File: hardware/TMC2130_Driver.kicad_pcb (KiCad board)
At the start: 2 copper layers, 36.7 x 39.4 mm, 35 parts, among them J1 PCIe_Stepper, J2 Conn_01x04_Male, J3 Screw_Terminal_01x02, U1 TMC2130, U2 24LC02

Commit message: 2130 completed
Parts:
- moved LOGO1 30.2 mm to (116.2, 78.0)
- moved JP1 22.6 mm to (117.5, 96.4)
- moved J3 22.2 mm to (141.5, 101.0), turned to 90 degrees
- moved C15 22.0 mm to (129.7, 77.7)
- moved C13 21.2 mm to (139.0, 80.6), turned to -90 degrees
- moved F1 20.8 mm to (135.6, 102.1), turned to 180 degrees
- moved R2 20.0 mm to (125.4, 77.9), turned to 180 degrees
- moved C4 19.9 mm to (132.8, 77.8), turned to 90 degrees
- moved J2 19.0 mm to (141.5, 87.0), turned to 90 degrees
- moved C17 19.0 mm to (130.9, 78.2), turned to 90 degrees
- moved C11 18.7 mm to (137.3, 81.4), turned to -90 degrees
- moved C5 15.8 mm to (126.2, 100.8), turned to 180 degrees
- moved C9 15.7 mm to (131.1, 80.7), turned to 0 degrees
- moved C3 15.5 mm to (133.7, 81.8), turned to 135 degrees
- moved C8 15.3 mm to (136.2, 83.7), turned to 0 degrees
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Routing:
- net /V_IO: track 17.3 -> 43.3 mm
- net /SCK: track 16.0 -> 38.6 mm, vias 1 -> 3
- net /CLOCK: track 20.7 -> 42.5 mm
- net /~CS: track 16.3 -> 36.0 mm
- net /V_HIGH: track 92.3 -> 75.5 mm
- net /5V: track 53.7 -> 70.5 mm
- net /MOSI: track 18.0 -> 34.0 mm
- net /MISO: track 17.7 -> 33.5 mm
- net /STEP: track 20.8 -> 35.8 mm
- net /ALARM1: track 33.6 -> 19.2 mm
- net /DIR: track 22.0 -> 35.2 mm
- net Net-(JP1-Pad1): track 23.0 -> 33.4 mm
- net GND: track 69.1 -> 61.3 mm, vias 61 -> 57
- net Net-(JP1-Pad3): track 22.8 -> 29.8 mm
- net /ID_0: track 8.53 -> 15.4 mm
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
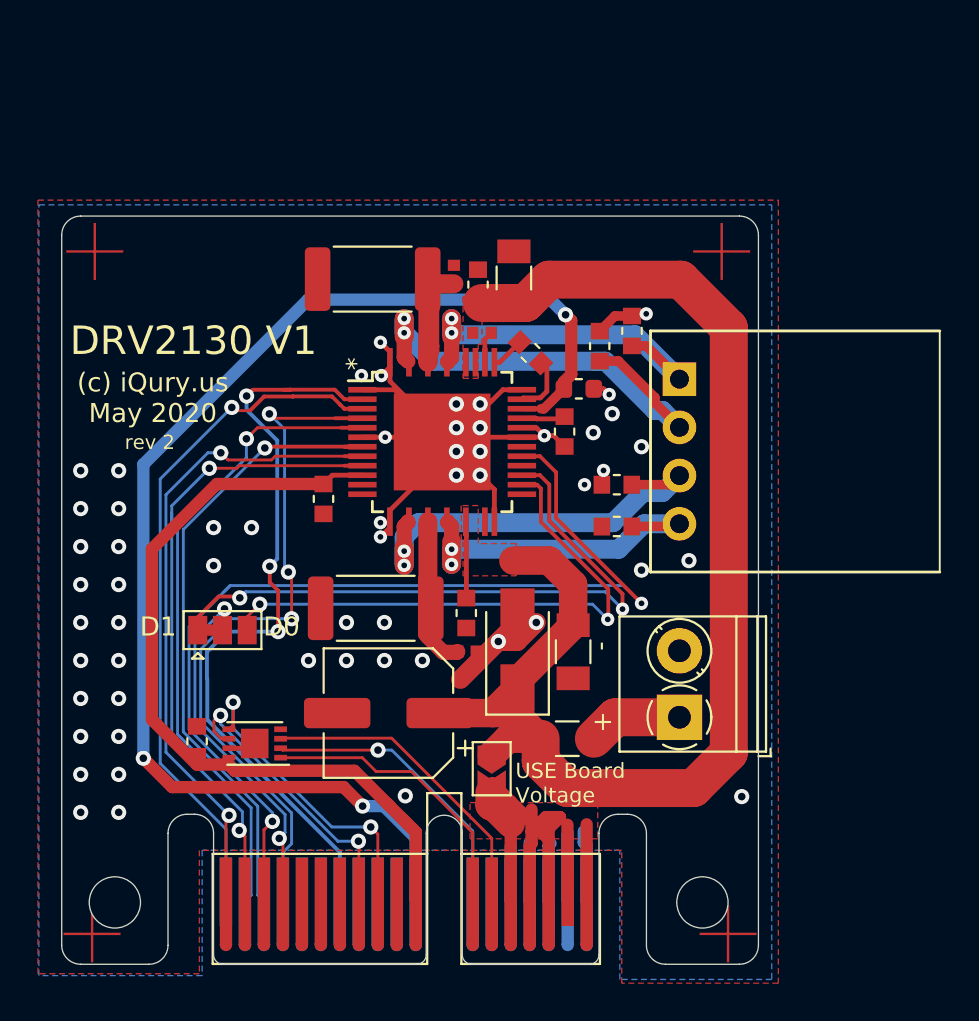
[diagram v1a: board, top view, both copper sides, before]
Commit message: Small correcion of 2130
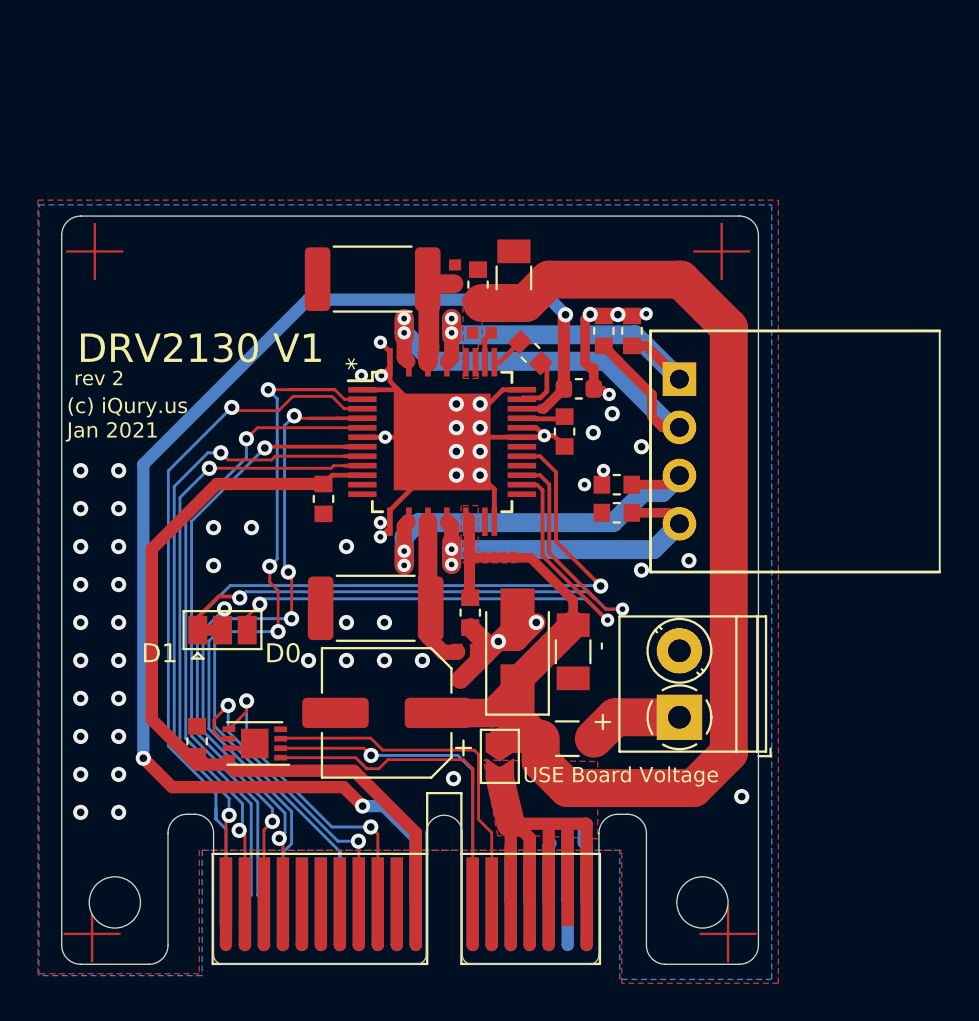
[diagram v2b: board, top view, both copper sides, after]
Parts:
- moved C11 0.83 mm to (137.6, 80.6)
- moved JP2 0.78 mm to (132.1, 103.0)
- moved C14 0.72 mm to (138.2, 90.2)
- moved C1 0.21 mm to (130.5, 95.5)
- moved C10 0.10 mm to (130.3, 97.4)
- moved C5 0.09 mm to (126.1, 100.8)
- moved C15 0.06 mm to (129.7, 77.7)
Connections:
- J1 pad : /STEP -> /CLOCK
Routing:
- net GND: track 61.3 -> 67.1 mm, vias 57 -> 60
- net /V_HIGH: track 75.5 -> 80.9 mm
- net /~ENABLE: track 53.0 -> 47.8 mm
- net /V_MOTORS: track 30.6 -> 27.4 mm
- net /ID_0: track 15.4 -> 18.5 mm
- net /5V: track 70.5 -> 67.7 mm
- net /ID_2: track 16.6 -> 18.8 mm
- net /SCK: track 38.6 -> 40.6 mm
- net /ID_1: track 15.6 -> 17.5 mm
- net /SCL: track 15.0 -> 16.4 mm
- net /V_IO: track 43.3 -> 42.0 mm
- net /DIR: track 35.2 -> 34.1 mm
- net /CLOCK: track 42.5 -> 43.4 mm
- net Net-(JP1-Pad1): track 33.4 -> 34.0 mm
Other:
- board text added: "(c) iQury.us Jan 2021"
- board text removed: "(c) iQury.us May 2020"
